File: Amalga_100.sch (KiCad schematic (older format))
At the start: 32 parts, among them P1 USB_B, P2 Interface, P3 IN+, P4 IN-, P5 MOTOR3, P6 MOTOR2, P7 MOTOR1, P9 CONN_6-HSWR-V2-rescue

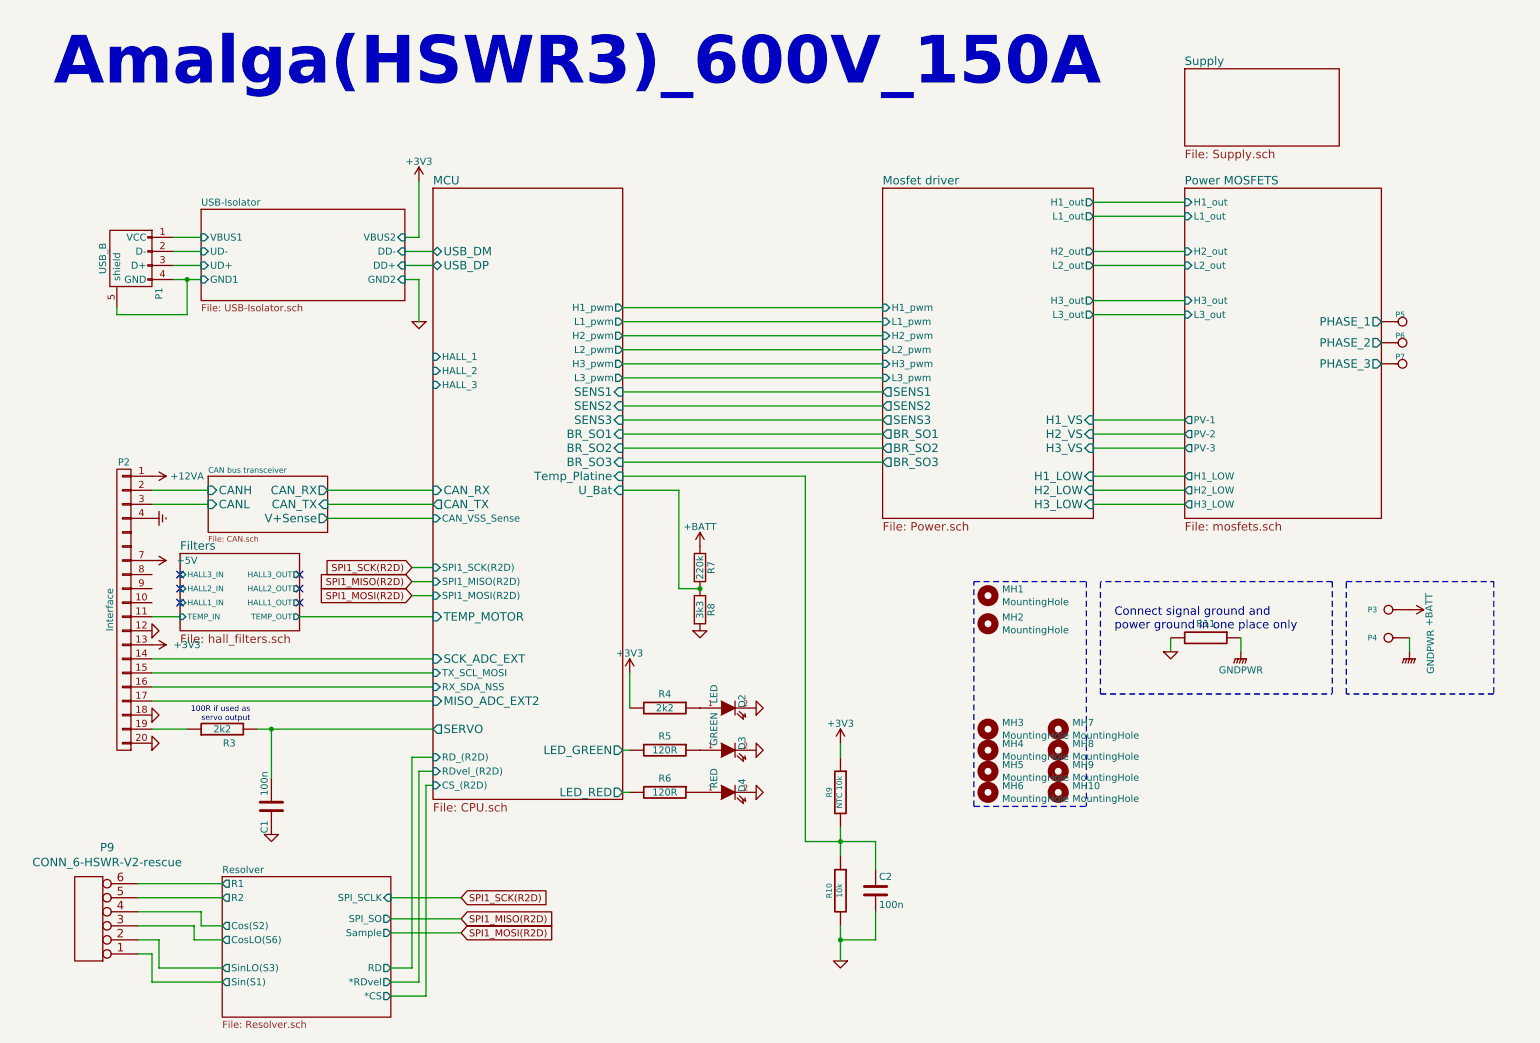
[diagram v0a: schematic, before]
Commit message: continued R2D AS1200 has encoder-interface
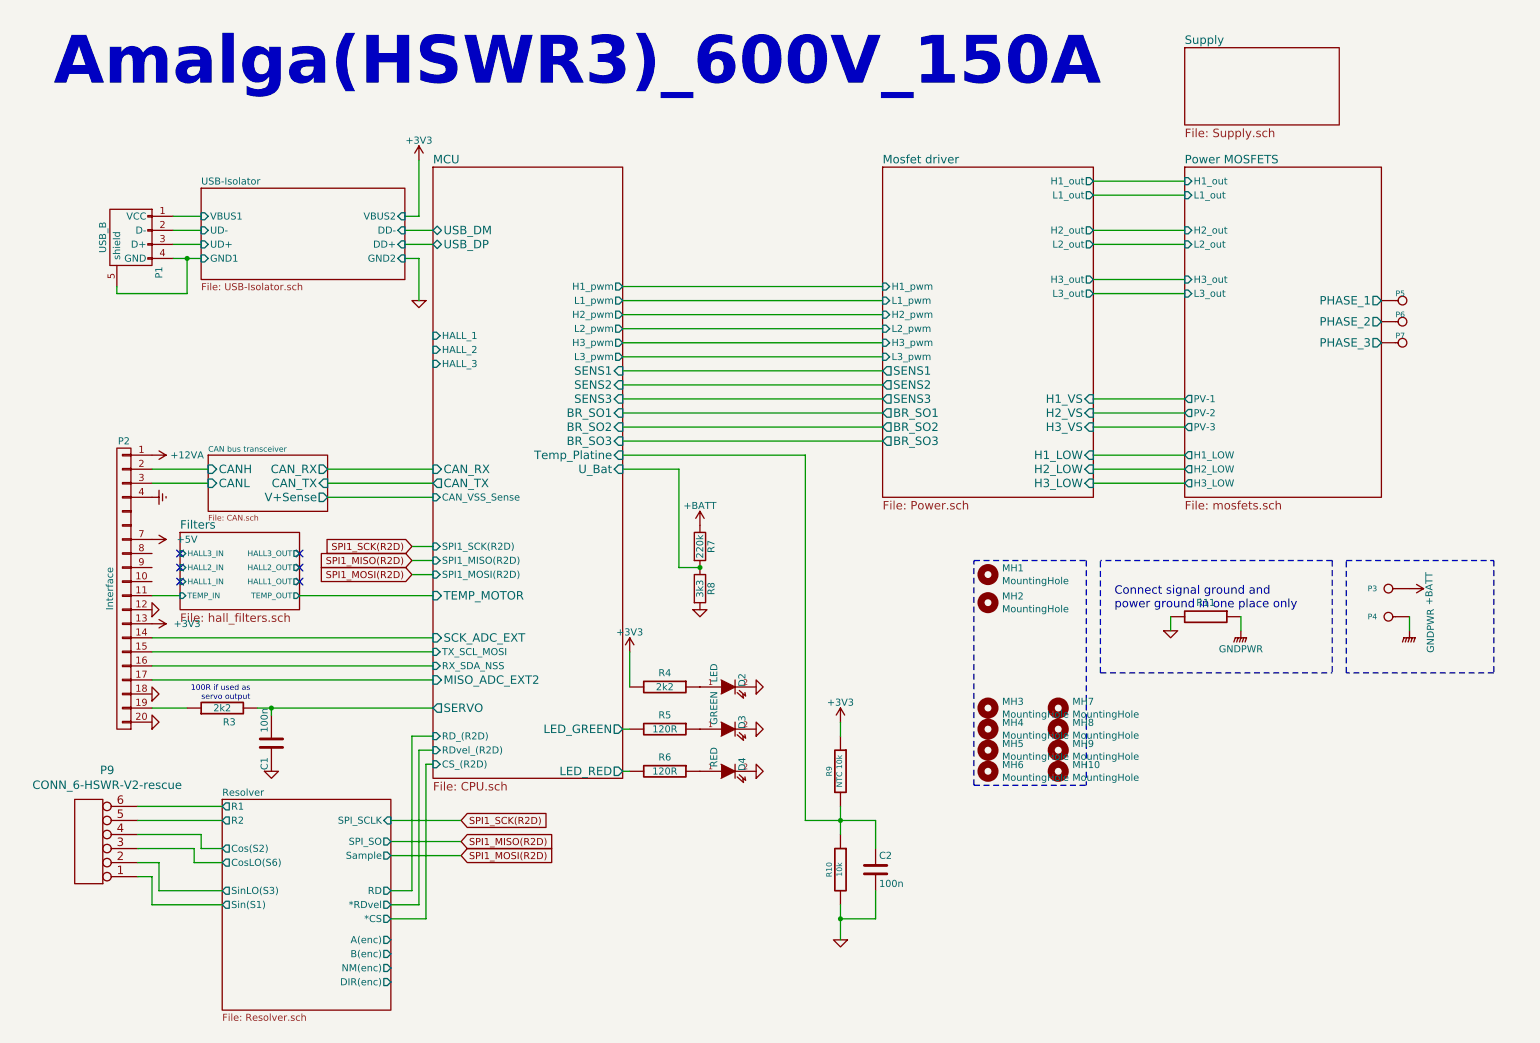
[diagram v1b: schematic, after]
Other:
- moved on the sheet: C1, C2, D2, D3, D4, MH1, MH10, MH2, MH3, MH4, MH5, MH6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

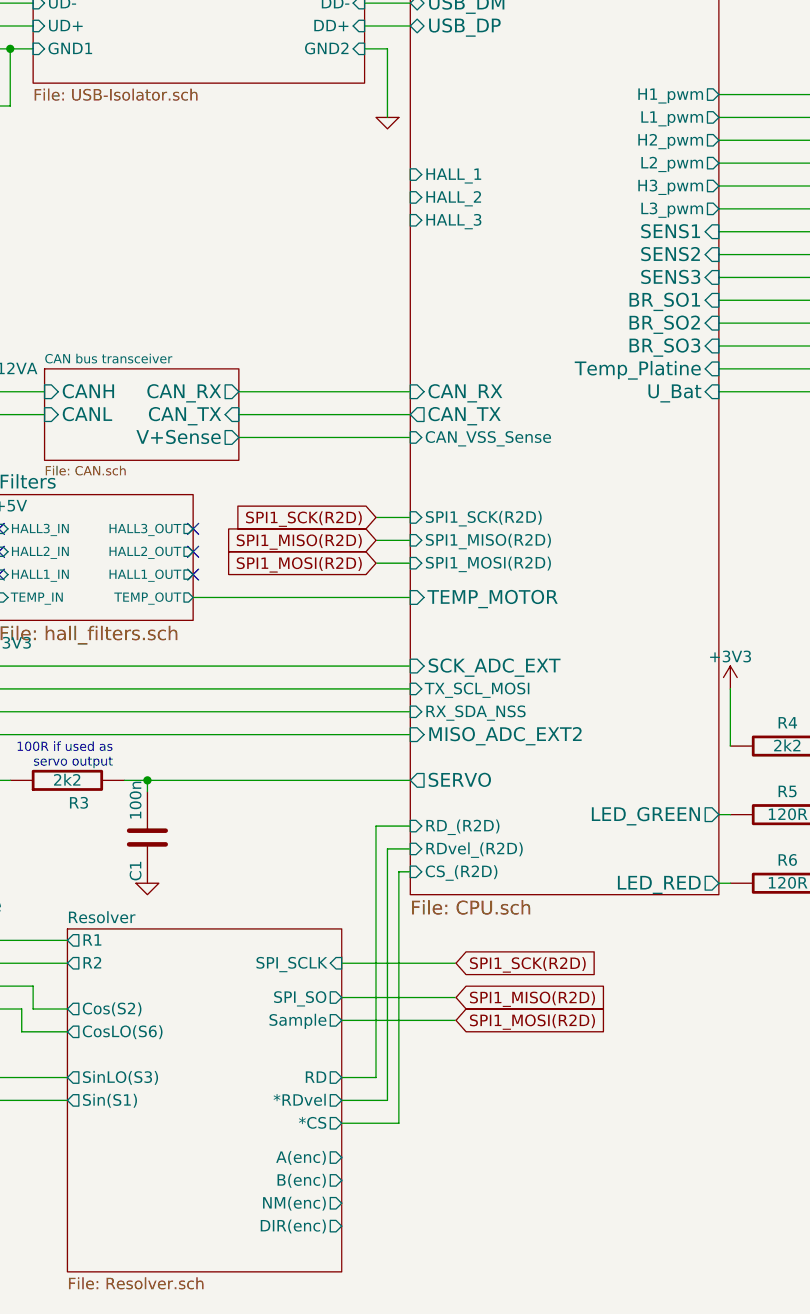
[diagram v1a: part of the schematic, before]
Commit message: continued Resolver continued Routing
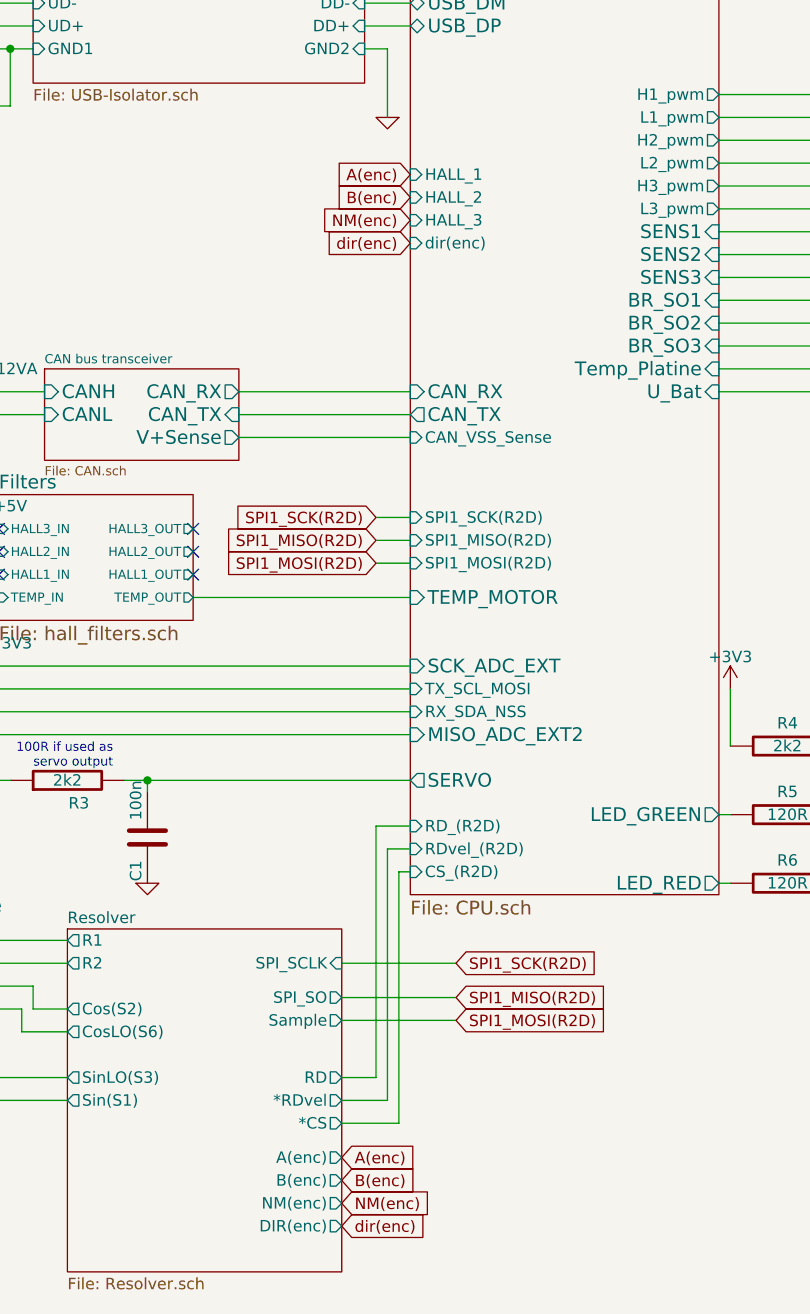
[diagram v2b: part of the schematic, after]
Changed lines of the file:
@@
 F36 "RDvel_(R2D)" I L 3300 5650 50
 F37 "RD_(R2D)" I L 3300 5550 50
+F38 "dir(enc)" I L 3300 3000 50
 $EndSheet
 Wire Wire Line
@@
 Wire Wire Line
 	2150 5350 3300 5350
+Text GLabel 3000 7000 2    50   Input ~ 0
+A(enc)
+Text GLabel 3000 7100 2    50   Input ~ 0
+B(enc)
+Text GLabel 3000 7200 2    50   Input ~ 0
+NM(enc)
+Text GLabel 3000 7300 2    50   Input ~ 0
+dir(enc)
+Text GLabel 3300 2700 0    50   Input ~ 0
+A(enc)
+Text GLabel 3300 2800 0    50   Input ~ 0
+B(enc)
+Text GLabel 3300 2900 0    50   Input ~ 0
+NM(enc)
+Text GLabel 3300 3000 0    50   Input ~ 0
+dir(enc)
 $EndSCHEMATC

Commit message: started with some changes. Whats to do: -R2D to 15V. -Hall-Filter -GND-decoupling by aperiodic caps -calculate R2D-Buffer gain -R2D gain semi switchable -frequency R2D switchable
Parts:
- removed R11: (no value), Resistor_SMD:R_0805_2012Metric, symbol Amalga_100-rescue:R-RESCUE-BLDC_4-HSWR-V2-rescue
- added JP? (x3): SolderJumper_3_Bridged12, symbol Jumper:SolderJumper_3_Bridged12
- added NT1: Net-Tie_2, NetTie:NetTie-2_SMD_Pad2.0mm, symbol Device:Net-Tie_2
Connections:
- wire segments 103 -> 117
- no-connect marks 6 -> 0
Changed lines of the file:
@@
 100R if used as\nservo output
 $Sheet
-S 1700 3550 850  400
+S 1800 3550 850  400
 U 5899E225
 F0 "CAN bus transceiver" 40
 F1 "CAN.sch" 40
-F2 "CAN_RX" O R 2550 3650 60
-F3 "CAN_TX" I R 2550 3750 60
-F4 "CANH" I L 1700 3650 60
-F5 "CANL" I L 1700 3750 60
-F6 "V+Sense" O R 2550 3850 60
+F2 "CAN_RX" O R 2650 3650 60
+F3 "CAN_TX" I R 2650 3750 60
+F4 "CANH" I L 1800 3650 60
+F5 "CANL" I L 1800 3750 60
+F6 "V+Sense" O R 2650 3850 60
 $EndSheet
 $Sheet
@@
 $EndComp
 Wire Wire Line
-	2550 3650 3300 3650
+	2650 3650 3300 3650
 Wire Wire Line
-	3300 3750 2550 3750
+	3300 3750 2650 3750
 Wire Wire Line
-	1700 3750 1300 3750
+	1800 3750 1300 3750
 Wire Wire Line
-	1300 3650 1700 3650
+	1300 3650 1800 3650
 Wire Wire Line
 	1300 4850 3300 4850
@@
 	1    0    0    -1
 $EndComp
-NoConn ~ 2350 4450
-NoConn ~ 2350 4350
-NoConn ~ 2350 4250
-NoConn ~ 1500 4250
-NoConn ~ 1500 4350
-NoConn ~ 1500 4450
 Wire Wire Line
-	3150 4200 3300 4200
+	3250 4200 3300 4200
 Wire Wire Line
-	3300 4300 3150 4300
+	3300 4300 3250 4300
 $Sheet
 S 3300 1500 1350 4350
@@
 F27 "SPI1_MISO(R2D)" I L 3300 4300 50
 F28 "SPI1_MOSI(R2D)" I L 3300 4400 50
-F29 "HALL_1" I L 3300 2700 50
-F30 "HALL_2" I L 3300 2800 50
-F31 "HALL_3" I L 3300 2900 50
+F29 "HALL_1" I L 3300 3250 50
+F30 "HALL_2" I L 3300 3100 50
+F31 "HALL_3" I L 3300 2950 50
 F32 "TX_SCL_MOSI" I L 3300 4950 50
 F33 "RX_SDA_NSS" I L 3300 5050 50
@@
 F36 "RDvel_(R2D)" I L 3300 5650 50
 F37 "RD_(R2D)" I L 3300 5550 50
-F38 "dir(enc)" I L 3300 3000 50
+F38 "dir(enc)" I L 3300 3400 50
 $EndSheet
 Wire Wire Line
 	4700 4950 4700 5200
-Text GLabel 3150 4200 0    50   Input ~ 0
+Text GLabel 3250 4200 0    50   Input ~ 0
 SPI1_SCK(R2D)
-Text GLabel 3150 4300 0    50   Input ~ 0
+Text GLabel 3250 4300 0    50   Input ~ 0
 SPI1_MISO(R2D)
-Text GLabel 3150 4400 0    50   Input ~ 0
+Text GLabel 3250 4400 0    50   Input ~ 0
 SPI1_MOSI(R2D)
 Wire Wire Line
-	3150 4400 3300 4400
+	3250 4400 3300 4400
 Text GLabel 3500 6150 2    50   Input ~ 0
 SPI1_SCK(R2D)
@@
 	8050 5100 9700 5100
 Wire Wire Line
-	2550 3850 3300 3850
+	2650 3850 3300 3850
 $Comp
 L Amalga_100-rescue:+3V3-power #PWR?
@@
 Wire Wire Line
 	3200 1450 3200 1850
-$Comp
-L Amalga_100-rescue:R-RESCUE-BLDC_4-HSWR-V2-rescue R11
-U 1 1 5CAE8AE9
-P 8800 4700
-F 0 "R11" V 8700 4700 50  0000 C CNN
-F 1 " " V 8800 4700 50  0000 C CNN
-F 2 "Resistor_SMD:R_0805_2012Metric" H 8800 4700 60  0001 C CNN
-F 3 "" H 8800 4700 60  0001 C CNN
-	1    8800 4700
-	0    1    1    0
-$EndComp
 Wire Wire Line
 	3300 5750 3250 5750
@@
 Text GLabel 3000 7300 2    50   Input ~ 0
 dir(enc)
-Text GLabel 3300 2700 0    50   Input ~ 0
+Text GLabel 2600 3050 1    50   Input ~ 0
 A(enc)
-Text GLabel 3300 2800 0    50   Input ~ 0
+Text GLabel 2500 2900 1    50   Input ~ 0
 B(enc)
-Text GLabel 3300 2900 0    50   Input ~ 0
+Text GLabel 2400 2750 1    50   Input ~ 0
 NM(enc)
-Text GLabel 3300 3000 0    50   Input ~ 0
+Text GLabel 3300 3400 0    50   Input ~ 0
 dir(enc)
+$Comp
+L Device:Net-Tie_2 NT1
+U 1 1 5CB51E34
+P 8800 4700
+F 0 "NT1" H 8800 4878 50  0000 C CNN
+F 1 "Net-Tie_2" H 8800 4787 50  0000 C CNN
+F 2 "NetTie:NetTie-2_SMD_Pad2.0mm" H 8800 4700 50  0001 C CNN
+F 3 "~" H 8800 4700 50  0001 C CNN
+	1    8800 4700
+	1    0    0    -1
+$EndComp
+Wire Wire Line
+	8700 4700 8550 4700
+Wire Wire Line
+	8900 4700 9050 4700
+Wire Wire Line
+	1300 4250 1500 4250
+Wire Wire Line
+	1300 4350 1500 4350
+Wire Wire Line
+	1300 4450 1500 4450
+Wire Wire Line
+	2350 4250 2400 4250
+Wire Wire Line
+	2350 4350 2500 4350
+Wire Wire Line
+	2350 4450 2600 4450
+Wire Wire Line
+	2600 4450 2600 3450
+$Comp
+L Jumper:SolderJumper_3_Bridged12 JP?
+U 1 1 5CB8C74E
+P 2600 3250
+F 0 "JP?" V 2554 3318 50  0000 L CNN
+F 1 "SolderJumper_3_Bridged12" V 2645 3318 50  0000 L CNN
+F 2 "" H 2600 3250 50  0001 C CNN
+F 3 "~" H 2600 3250 50  0001 C CNN
+	1    2600 3250
+	0    -1   1    0
+$EndComp
+$Comp
+L Jumper:SolderJumper_3_Bridged12 JP?
+U 1 1 5CBCA381
+P 2400 2950
+F 0 "JP?" V 2354 3018 50  0000 L CNN
+F 1 "SolderJumper_3_Bridged12" V 2445 3018 50  0000 L CNN
+F 2 "" H 2400 2950 50  0001 C CNN
+F 3 "~" H 2400 2950 50  0001 C CNN
+	1    2400 2950
+	0    -1   1    0
+$EndComp
+$Comp
+L Jumper:SolderJumper_3_Bridged12 JP?
+U 1 1 5CBC521D
+P 2500 3100
+F 0 "JP?" V 2454 3168 50  0000 L CNN
+F 1 "SolderJumper_3_Bridged12" V 2545 3168 50  0000 L CNN
+F 2 "" H 2500 3100 50  0001 C CNN
+F 3 "~" H 2500 3100 50  0001 C CNN
+	1    2500 3100
+	0    -1   1    0
+$EndComp
+Wire Wire Line
+	2500 3300 2500 4350
+Wire Wire Line
+	2400 3150 2400 4250
+Wire Wire Line
+	2750 3250 3300 3250
+Wire Wire Line
+	2650 3100 3300 3100
+Wire Wire Line
+	2550 2950 3300 2950
 $EndSCHEMATC

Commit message: -added some more caps espacially decoupling-caps -little changes
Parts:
- added C45, C46, C48: 100n, Capacitor_SMD:C_0805_2012Metric, symbol Amalga_100-rescue:C-Device
- JP1, JP2, JP3: renamed from JP?; footprint (none) -> Jumper:SolderJumper-3_P1.3mm_Bridged12_RoundedPad1.0x1.5mm
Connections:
- wire segments 117 -> 129
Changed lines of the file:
@@
 L Amalga_100-rescue:GND-RESCUE-BLDC_4-HSWR-V2-rescue #PWR01
 U 1 1 5895E67B
-P 8550 4800
-F 0 "#PWR01" H 8550 4800 30  0001 C CNN
-F 1 "GND" H 8550 4730 30  0001 C CNN
-F 2 "" H 8550 4800 60  0001 C CNN
-F 3 "" H 8550 4800 60  0001 C CNN
-	1    8550 4800
+P 8550 5700
+F 0 "#PWR01" H 8550 5700 30  0001 C CNN
+F 1 "GND" H 8550 5630 30  0001 C CNN
+F 2 "" H 8550 5700 60  0001 C CNN
+F 3 "" H 8550 5700 60  0001 C CNN
+	1    8550 5700
 	1    0    0    -1
 $EndComp
@@
 	8000 3750 8650 3750
 Wire Wire Line
-	8550 4700 8550 4800
+	8550 4700 8550 4900
 Wire Wire Line
-	9050 4700 9050 4800
+	9050 4700 9050 4900
 Wire Wire Line
 	10250 4800 10250 4700
@@
 L Amalga_100-rescue:GNDPWR-HSWR-V2-rescue #PWR02
 U 1 1 5895E699
-P 9050 4800
-F 0 "#PWR02" H 9050 4600 50  0001 C CNN
-F 1 "GNDPWR" H 9050 4670 50  0000 C CNN
-F 2 "" H 9050 4750 50  0000 C CNN
-F 3 "" H 9050 4750 50  0000 C CNN
-	1    9050 4800
+P 9050 5650
+F 0 "#PWR02" H 9050 5450 50  0001 C CNN
+F 1 "GNDPWR" H 9050 5520 50  0000 C CNN
+F 2 "" H 9050 5600 50  0000 C CNN
+F 3 "" H 9050 5600 50  0000 C CNN
+	1    9050 5650
 	1    0    0    -1
 $EndComp
@@
 $EndComp
 Wire Notes Line
-	9700 4300 9700 5100
+	9700 4300 9700 5900
 Wire Notes Line
-	8050 5100 8050 4300
+	8050 5900 8050 4300
 Wire Notes Line
 	9700 4300 8050 4300
@@
 	7150 5900 7950 5900
 Wire Notes Line
-	8050 5100 9700 5100
+	8050 5900 9700 5900
 Wire Wire Line
 	2650 3850 3300 3850
@@
 	2600 4450 2600 3450
 $Comp
-L Jumper:SolderJumper_3_Bridged12 JP?
+L Jumper:SolderJumper_3_Bridged12 JP3
 U 1 1 5CB8C74E
 P 2600 3250
-F 0 "JP?" V 2554 3318 50  0000 L CNN
+F 0 "JP3" V 2554 3318 50  0000 L CNN
 F 1 "SolderJumper_3_Bridged12" V 2645 3318 50  0000 L CNN
-F 2 "" H 2600 3250 50  0001 C CNN
+F 2 "Jumper:SolderJumper-3_P1.3mm_Bridged12_RoundedPad1.0x1.5mm" H 2600 3250 50  0001 C CNN
 F 3 "~" H 2600 3250 50  0001 C CNN
 	1    2600 3250
@@
 $EndComp
 $Comp
-L Jumper:SolderJumper_3_Bridged12 JP?
+L Jumper:SolderJumper_3_Bridged12 JP1
 U 1 1 5CBCA381
 P 2400 2950
-F 0 "JP?" V 2354 3018 50  0000 L CNN
+F 0 "JP1" V 2354 3018 50  0000 L CNN
 F 1 "SolderJumper_3_Bridged12" V 2445 3018 50  0000 L CNN
-F 2 "" H 2400 2950 50  0001 C CNN
+F 2 "Jumper:SolderJumper-3_P1.3mm_Bridged12_RoundedPad1.0x1.5mm" H 2400 2950 50  0001 C CNN
 F 3 "~" H 2400 2950 50  0001 C CNN
 	1    2400 2950
@@
 $EndComp
 $Comp
-L Jumper:SolderJumper_3_Bridged12 JP?
+L Jumper:SolderJumper_3_Bridged12 JP2
 U 1 1 5CBC521D
 P 2500 3100
-F 0 "JP?" V 2454 3168 50  0000 L CNN
+F 0 "JP2" V 2454 3168 50  0000 L CNN
 F 1 "SolderJumper_3_Bridged12" V 2545 3168 50  0000 L CNN
-F 2 "" H 2500 3100 50  0001 C CNN
+F 2 "Jumper:SolderJumper-3_P1.3mm_Bridged12_RoundedPad1.0x1.5mm" H 2500 3100 50  0001 C CNN
 F 3 "~" H 2500 3100 50  0001 C CNN
 	1    2500 3100
@@
 Wire Wire Line
 	2550 2950 3300 2950
+$Comp
+L Amalga_100-rescue:C-Device C45
+U 1 1 5CB814BD
+P 8800 4900
+F 0 "C45" H 8825 5000 50  0000 L CNN
+F 1 "100n" H 8825 4800 50  0000 L CNN
+F 2 "Capacitor_SMD:C_0805_2012Metric" H 8838 4750 50  0001 C CNN
+F 3 "" H 8800 4900 50  0000 C CNN
+	1    8800 4900
+	0    1    1    0
+$EndComp
+$Comp
+L Amalga_100-rescue:C-Device C46
+U 1 1 5CB86C31
+P 8800 5150
+F 0 "C46" H 8825 5250 50  0000 L CNN
+F 1 "100n" H 8825 5050 50  0000 L CNN
+F 2 "Capacitor_SMD:C_0805_2012Metric" H 8838 5000 50  0001 C CNN
+F 3 "" H 8800 5150 50  0000 C CNN
+	1    8800 5150
+	0    1    1    0
+$EndComp
+$Comp
+L Amalga_100-rescue:C-Device C48
+U 1 1 5CBA6759
+P 8800 5450
+F 0 "C48" H 8825 5550 50  0000 L CNN
+F 1 "100n" H 8825 5350 50  0000 L CNN
+F 2 "Capacitor_SMD:C_0805_2012Metric" H 8838 5300 50  0001 C CNN
+F 3 "" H 8800 5450 50  0000 C CNN
+	1    8800 5450
+	0    1    1    0
+$EndComp
+Wire Wire Line
+	8950 5450 9050 5450
+Connection ~ 9050 5450
+Wire Wire Line
+	9050 5450 9050 5650
+Wire Wire Line
+	8950 5150 9050 5150
+Connection ~ 9050 5150
+Wire Wire Line
+	9050 5150 9050 5450
+Wire Wire Line
+	8950 4900 9050 4900
+Connection ~ 9050 4900
+Wire Wire Line
+	9050 4900 9050 5150
+Wire Wire Line
+	8650 4900 8550 4900
+Connection ~ 8550 4900
+Wire Wire Line
+	8550 4900 8550 5150
+Wire Wire Line
+	8650 5150 8550 5150
+Connection ~ 8550 5150
+Wire Wire Line
+	8550 5150 8550 5450
+Wire Wire Line
+	8650 5450 8550 5450
+Connection ~ 8550 5450
+Wire Wire Line
+	8550 5450 8550 5700
+$Comp
+L Graphic:SYM_ESD_Small #SYM?
+U 1 1 5CCA21D9
+P 3850 2600
+F 0 "#SYM?" H 3850 2740 50  0001 C CNN
+F 1 "SYM_ESD_Small" H 3850 2475 50  0001 C CNN
+F 2 "" H 3850 2610 50  0001 C CNN
+F 3 "~" H 3850 2610 50  0001 C CNN
+	1    3850 2600
+	1    0    0    -1
+$EndComp
 $EndSCHEMATC
